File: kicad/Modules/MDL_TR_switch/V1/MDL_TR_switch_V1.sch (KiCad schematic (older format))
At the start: 3 parts

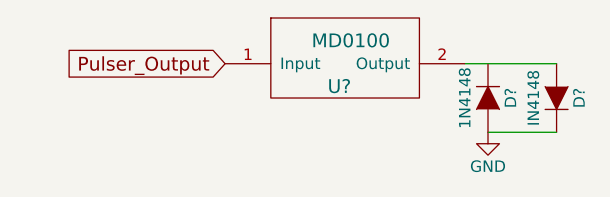
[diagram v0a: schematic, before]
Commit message: adding MDL_TGC
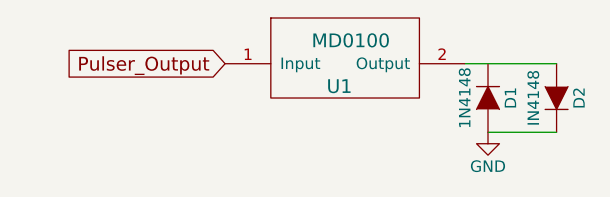
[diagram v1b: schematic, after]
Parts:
- gave numbers to parts that had none: 3
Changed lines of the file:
@@
 LIBS:valves
 LIBS:echopen
+LIBS:MDL_TR_switch_V1-cache
 EELAYER 25 0
 EELAYER END
@@
 $EndDescr
 $Comp
-L MD0100 U?
+L MD0100 U1
 U 1 1 57A4ADCE
 P 4450 2900
-F 0 "U?" H 4400 2850 60  0000 C CNN
+F 0 "U1" H 4400 2850 60  0000 C CNN
 F 1 "MD0100" H 4450 3050 60  0000 C CNN
 F 2 "" H 4450 2900 60  0000 C CNN
@@
 Pulser_Output
 $Comp
-L D D?
+L D D1
 U 1 1 57A4AE58
 P 5050 3000
-F 0 "D?" H 5050 3100 50  0000 C CNN
+F 0 "D1" H 5050 3100 50  0000 C CNN
 F 1 "1N4148" H 5050 2900 50  0000 C CNN
 F 2 "" H 5050 3000 50  0000 C CNN
@@
 $EndComp
 $Comp
-L D D?
+L D D2
 U 1 1 57A4AEBB
 P 5350 3000
-F 0 "D?" H 5350 3100 50  0000 C CNN
+F 0 "D2" H 5350 3100 50  0000 C CNN
 F 1 "IN4148" H 5350 2900 50  0000 C CNN
 F 2 "" H 5350 3000 50  0000 C CNN
@@
 	5050 3150 5350 3150
 $Comp
-L GND #PWR?
+L GND #PWR01
 U 1 1 57A4AFC1
 P 5050 3150
-F 0 "#PWR?" H 5050 2900 50  0001 C CNN
+F 0 "#PWR01" H 5050 2900 50  0001 C CNN
 F 1 "GND" H 5050 3000 50  0000 C CNN
 F 2 "" H 5050 3150 50  0000 C CNN
